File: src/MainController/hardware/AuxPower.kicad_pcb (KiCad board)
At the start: 2 copper layers, 90 x 90 mm, 123 parts, among them J1 MC 1,5/2, J10 MC 1,5/4, J11 S3B-XH-A, J12 S3B-XH-A, J13 S3B-XH-A, J14 S3B-XH-A, J15 S3B-XH-A, J16 B3B-XH-A, J17 B4B-XH-A, J2 MC 1,5/2, J3 MC 1,5/2, J4 MC 1,5/2, J5 MC 1,5/2, J6 MC 1,5/4, J7 MC 1,5/4, J8 MC 1,5/4, J9 MC 1,5/4, Q1 BC846B,235, Q10 RS3L110, Q2 BC846B,235, Q3 BC846B,235, Q4 BC846B,235, Q5 BC846B,235, Q6 RS3L110, Q7 RS3L110, Q8 RS3L110, Q9 RS3L110, U1 ZXCT1009, U2 ZXCT1009, U3 ZXCT1009, U4 ZXCT1009, U5 ZXCT1009, U6 PIC18F26K83, U7 PI4IOE5V6416, U8 MCP9701

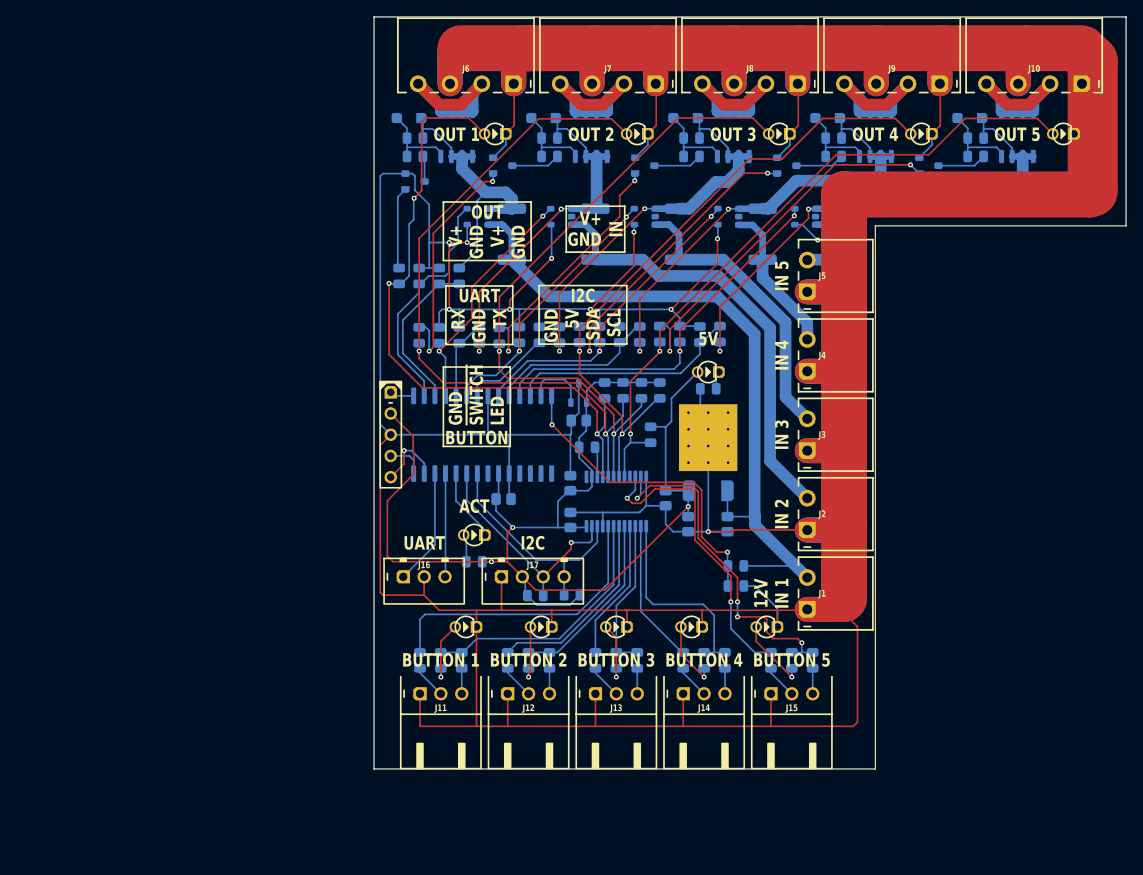
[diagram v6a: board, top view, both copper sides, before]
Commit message: Refactoring to use PhotoMOS (not completed)
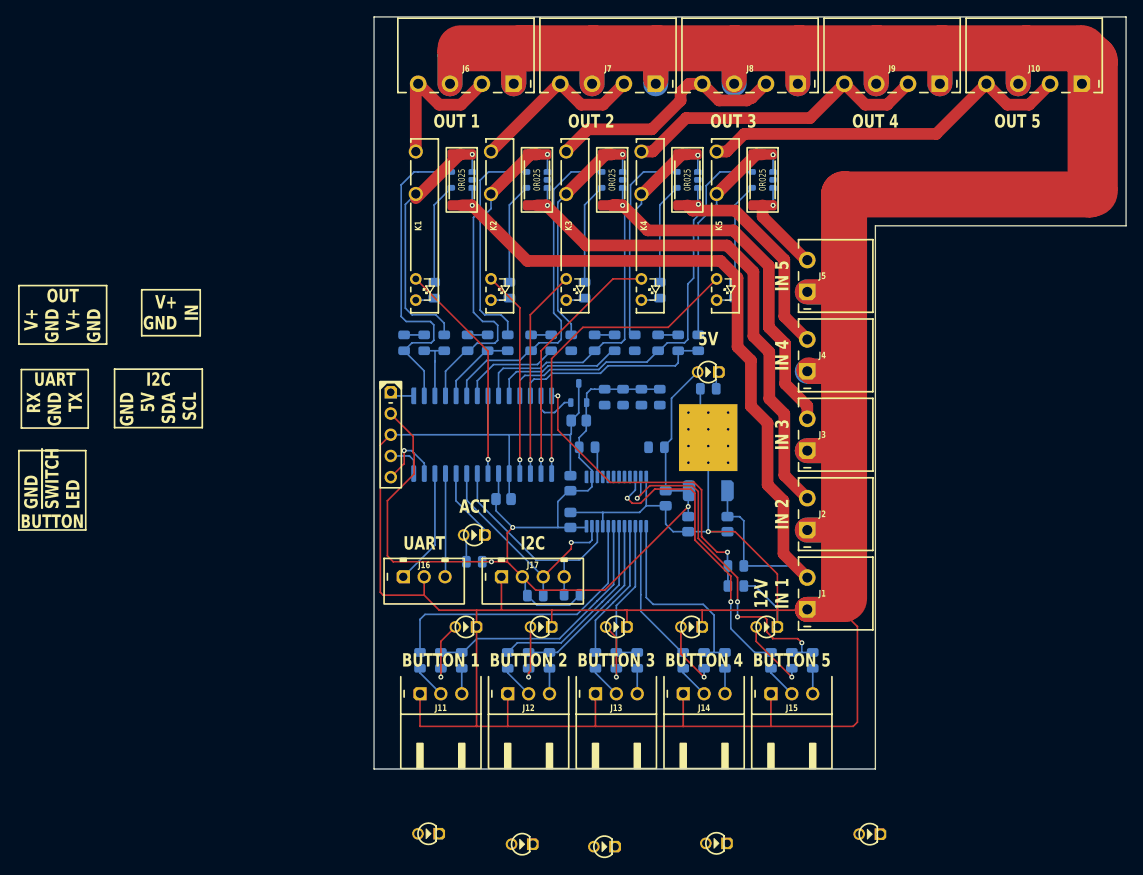
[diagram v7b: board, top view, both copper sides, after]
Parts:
- removed D1, D2, D3, D4, D5: BZT52C12, Medo64:D Zener (SOD123FL)
- removed Q1, Q2, Q3, Q4, Q5: BC846B,235, Medo64:Q Transistor NPN (SOT23-3)
- removed Q10, Q6, Q7, Q8, Q9: RS3L110, Medo64:Q MOSFET-P (SO-8)
- removed the R47 at (19.9, 31.7)
- removed the R48 at (36.0, 31.7)
- removed the R49 at (53.0, 31.7)
- removed the R50 at (70.0, 31.7)
- removed the R51 at (87.0, 31.7)
- removed R53, R54, R55, R56, R57: 62K, Medo64:R (0805)
- added K1: AQZ202G, Medo64:K PhotoMOS [AQZ202G], F.Cu at (20.0, 40.0)
- added K2: AQZ202G, Medo64:K PhotoMOS [AQZ202G], F.Cu at (29.0, 40.0)
- added K3: AQZ202G, Medo64:K PhotoMOS [AQZ202G], F.Cu at (38.0, 40.0)
- added K4: AQZ202G, Medo64:K PhotoMOS [AQZ202G], F.Cu at (47.0, 40.0)
- added K5: AQZ202G, Medo64:K PhotoMOS [AQZ202G], F.Cu at (56.0, 40.0)
- R1, R2, R3, R4, R5: moved to F.Cu
- R16: renamed from R42; value 10K -> 1K5
- R17: renamed from R43; value 10K -> 1K5
- R18: renamed from R44; value 10K -> 1K5
- R19: renamed from R45; value 10K -> 1K5
- R20: renamed from R46; value 10K -> 1K5
- moved DS9 88.4 mm to (56.0, 113.9)
- moved DS8 87.8 mm to (42.6, 114.3)
- moved DS10 86.9 mm to (74.3, 112.8)
- moved DS7 86.1 mm to (32.7, 114.0)
- moved DS6 84.1 mm to (21.5, 112.8)
- moved R17 12.1 mm to (31.2, 47.7), turned to -90 degrees
- moved R18 11.6 mm to (40.2, 47.7), turned to -90 degrees
- moved R5 11.3 mm to (61.5, 34.5)
- moved R4 11.1 mm to (52.5, 34.5)
- moved R19 11.0 mm to (49.2, 47.7), turned to -90 degrees
- moved R20 10.4 mm to (58.2, 47.7), turned to -90 degrees
- moved R3 10.3 mm to (43.5, 34.5)
- moved R2 9.55 mm to (34.5, 34.5)
- moved R1 8.85 mm to (25.5, 34.5)
- moved R41 8.20 mm to (21.0, 54.0)
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- renumbered R16 to R21, R17 to R22, R18 to R23, R19 to R24, R20 to R25, R21 to R26, R22 to R27, R23 to R28, R24 to R29, R25 to R30, R26 to R31, R27 to R32, R28 to R33, R29 to R34, R30 to R35, R31 to R36, R32 to R37, R33 to R38, R34 to R39, R35 to R40, R36 to R41, R37 to R42, R38 to R43, R39 to R44, R40 to R45, R41 to R46, R52 to R47, R58 to R48, R59 to R49, R60 to R50, R61 to R51, R62 to R52
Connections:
- R16 pad 1: BASE1 -> OUT_OUTPUT1'
- R16 pad 2: OUT_OUTPUT1 -> GND
- R17 pad 1: OUT_OUTPUT2 -> GND
- R17 pad 2: BASE2 -> OUT_OUTPUT2'
- R18 pad 1: OUT_OUTPUT3 -> GND
- R18 pad 2: BASE3 -> OUT_OUTPUT3'
- R19 pad 1: OUT_OUTPUT4 -> GND
- R19 pad 2: BASE4 -> OUT_OUTPUT4'
- R20 pad 1: OUT_OUTPUT5 -> GND
- R20 pad 2: BASE5 -> OUT_OUTPUT5'
- U6 pad 15: (no net) -> OUT_OUTPUT5
- U6 pad 16: (no net) -> OUT_OUTPUT4
- U6 pad 17: (no net) -> OUT_OUTPUT3
- U6 pad 18: (no net) -> OUT_OUTPUT2
- U6 pad 21: (no net) -> OUT_OUTPUT1
- U7 pad 4: OUT_OUTPUT1 -> (no net)
- U7 pad 5: OUT_OUTPUT2 -> (no net)
- U7 pad 6: OUT_OUTPUT3 -> (no net)
- U7 pad 7: OUT_OUTPUT4 -> (no net)
- U7 pad 8: OUT_OUTPUT5 -> (no net)
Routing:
- net GND: track 924.7 -> 801.3 mm, vias 11 -> 1
- net OUT_OUTPUT2: track 84.8 -> 24.7 mm, vias 2 -> 1
- net OUT_OUTPUT3: track 80.7 -> 25.1 mm, vias 2 -> 1
- net OUT_OUTPUT1: track 79.1 -> 26.9 mm, vias 3 -> 1
- net OUT_OUTPUT4: track 78.0 -> 30.3 mm, vias 2 -> 1
- net BASE5: track 45.2 -> 0.00 mm, vias 2 -> 0
- net OUT_OUTPUT5: track 81.1 -> 37.5 mm, vias 2 -> 1
- net BASE4: track 37.1 -> 0.00 mm, vias 2 -> 0
- net INPUT5': track 63.6 -> 27.3 mm, vias 2 -> 1
- net BASE3: track 31.5 -> 0.00 mm, vias 2 -> 0
- net BASE2: track 28.8 -> 0.00 mm, vias 2 -> 0
- net INPUT4': track 54.7 -> 27.5 mm, vias 2 -> 1
- net OUTPUT5: track 21.7 -> 45.3 mm
- net INPUT3': track 47.4 -> 27.8 mm, vias 2 -> 1
- net OUTPUT4: track 21.7 -> 37.3 mm
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
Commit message: Reconnected all broken traces
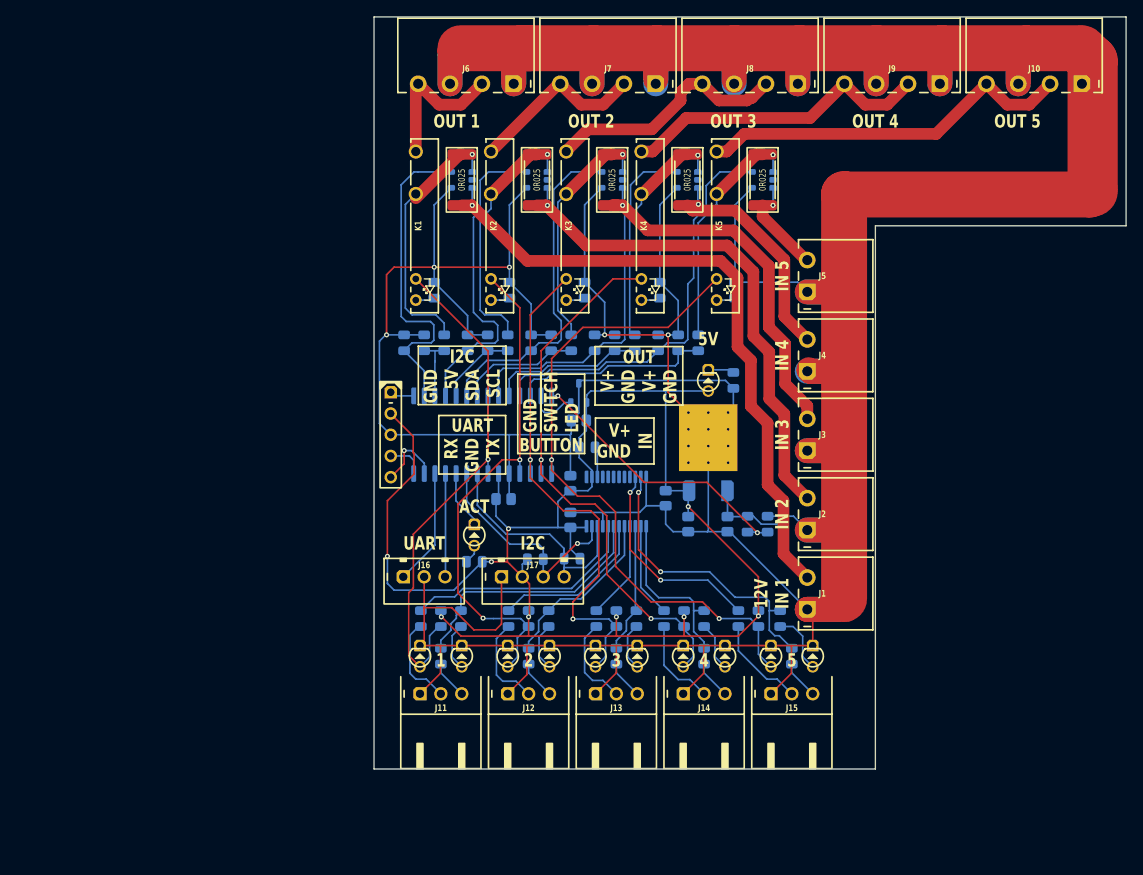
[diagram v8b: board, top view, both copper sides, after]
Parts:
- moved R22 33.0 mm to (23.0, 87.0)
- moved R23 28.8 mm to (33.5, 87.0)
- moved R24 26.7 mm to (44.0, 87.0)
- moved R25 26.7 mm to (52.1, 87.0)
- moved DS10 24.4 mm to (62.5, 91.5), turned to -90 degrees
- moved R26 23.9 mm to (61.0, 87.0), turned to -90 degrees
- moved DS8 22.8 mm to (41.5, 91.5), turned to -90 degrees
- moved DS9 22.8 mm to (52.0, 91.5), turned to -90 degrees
- moved DS7 22.6 mm to (31.0, 91.5), turned to -90 degrees
- moved DS6 21.3 mm to (20.5, 91.5), turned to -90 degrees
- moved R46 8.32 mm to (62.1, 75.7), turned to 90 degrees
- moved DS5 6.52 mm to (67.5, 91.5), turned to -90 degrees
- moved R38 6.34 mm to (58.6, 87.0)
- moved R27 5.55 mm to (35.9, 87.0)
- moved R28 5.55 mm to (46.4, 87.0)
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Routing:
- net 5V: track 142.1 -> 192.9 mm, vias 3 -> 9
- net OUT_OUTPUT5: track 37.5 -> 80.5 mm, vias 1 -> 2
- net OUT_OUTPUT3: track 25.1 -> 62.2 mm, vias 1 -> 2
- net OUT_OUTPUT2: track 24.7 -> 60.9 mm, vias 1 -> 2
- net OUT_OUTPUT4: track 30.3 -> 66.2 mm, vias 1 -> 2
- net OUT_OUTPUT1: track 26.9 -> 61.8 mm
- net GND: track 801.3 -> 825.7 mm, vias 1 -> 5
- net IN_BUTTON5_SWITCH: track 36.2 -> 24.9 mm
- net BUTTON5_SWITCH: track 4.09 -> 11.4 mm
- net BUTTON2_SWITCH: track 4.09 -> 11.2 mm
- net BUTTON3_SWITCH: track 4.09 -> 10.9 mm
- net BUTTON4_SWITCH: track 4.09 -> 10.9 mm
- net IN_BUTTON1_SWITCH: track 35.1 -> 28.4 mm
- net BUTTON1_SWITCH: track 4.09 -> 10.7 mm
- net OUT_BUTTON5_LED: track 41.5 -> 35.4 mm, vias 4 -> 2
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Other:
- board text removed: "BUTTON 1"
- board text removed: "BUTTON 2"
- board text removed: "BUTTON 3"
- board text removed: "BUTTON 4"
- board text removed: "BUTTON 5"
